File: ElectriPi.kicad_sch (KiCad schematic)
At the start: 56 parts, among them IC2 TPS51397ARJER, J1 2444, J2 JST XH 01x02, J3 JST XH 01x02, J6 Raspberry_Pi_2_3, J8 JST XH 01x02, Q1 SiA471DJ, Q2 SiA430DJT, U1 LM74700, U2 COOLING

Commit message: Add DigiKey PN's
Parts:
- C1, C11, C12, C2: DigiKey (none) -> 445-14428-2-ND
- C10, C13, C14, C15, C17, C6, C7, C8, C9: DigiKey (none) -> 490-GRM155R62A104KE14JTR-ND
- C18: DigiKey (none) -> 399-EEV107M050S9MAATR-ND
- C3: DigiKey (none) -> 1276-1860-2-ND
- C4, C5: DigiKey (none) -> 490-GRM31CR61A107MEA8KTR-ND
- D1: DigiKey (none) -> 112-XMC7K24CAHM3/ITR-ND
- D3, D5: DigiKey (none) -> 754-1124-2-ND
- D4: DigiKey (none) -> BZX84C13-FDITR-ND
- D6: DigiKey (none) -> 1727-2175-1-ND
- F1: DigiKey (none) -> F1889-ND
- IC2: DigiKey (none) -> 296-TPS51397ARJERTR-ND
- J2: DigiKey (none) -> 455-B2B-XH-A-ND
- L1: DigiKey (none) -> 541-1313-2-ND
- Q1: DigiKey (none) -> SIA471DJ-T1-GE3TR-ND
- Q2: DigiKey (none) -> 742-SIA430DJT-T1-GE3CT-ND
- R1, R11, R5: DigiKey (none) -> CR0402-FX-3302GLFTR-ND
- R12, R13, R7: DigiKey (none) -> CR0402-FX-1103GLFTR-ND
- R14: DigiKey (none) -> CR0402-FX-1502GLFTR-ND
- R3: DigiKey (none) -> CR0402-FX-1103GLFTR-ND; abv.Footprint 0402 -> (none)
- R4: DigiKey (none) -> CR0402-FX-1803GLFTR-ND
- R6: DigiKey (none) -> 311-1.00KLRTR-ND
- R8: DigiKey (none) -> CR0402-FX-1002GLFTR-ND
- U1: DigiKey (none) -> 296-LM74700QDBVRQ1CT-ND
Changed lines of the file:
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@@
+      (effects (font (size 1.27 1.27)) hide)
+    )
+    (property "DigiKey" "490-GRM155R62A104KE14JTR-ND" (at 102.235 43.18 0)
       (effects (font (size 1.27 1.27)) hide)
     )
@@
       (effects (font (size 1.27 1.27)) hide)
     )
+    (property "DigiKey" "754-1124-2-ND" (at 33.02 177.8 0)
+      (effects (font (size 1.27 1.27)) hide)
+    )
     (pin "1")
     (pin "2")
@@
     )
     (property "LCSC" "C1518754" (at 110.49 59.69 0)
+      (effects (font (size 1.27 1.27)) hide)
+    )
+    (property "DigiKey" "296-TPS51397ARJERTR-ND" (at 110.49 59.69 0)
       (effects (font (size 1.27 1.27)) hide)
     )
@@
       (effects (font (size 1.27 1.27)) hide)
     )
+    (property "DigiKey" "BZX84C13-FDITR-ND" (at 67.31 54.61 90)
+      (effects (font (size 1.27 1.27)) hide)
+    )
     (pin "1")
     (pin "2")
@@
     )
     (property "LCSC" "C2193622" (at 22.86 62.23 0)
+      (effects (font (size 1.27 1.27)) hide)
+    )
+    (property "DigiKey" "490-GRM155R62A104KE14JTR-ND" (at 22.86 62.23 0)
       (effects (font (size 1.27 1.27)) hide)
     )
@@
       (effects (font (size 1.27 1.27)) hide)
     )
+    (property "DigiKey" "490-GRM155R62A104KE14JTR-ND" (at 153.67 127 0)
+      (effects (font (size 1.27 1.27)) hide)
+    )
     (pin "1")
     (pin "2")
@@
       (effects (font (size 1.27 1.27)) hide)
     )
+    (property "DigiKey" "490-GRM155R62A104KE14JTR-ND" (at 186.69 55.88 0)
+      (effects (font (size 1.27 1.27)) hide)
+    )
     (pin "1")
     (pin "2")
@@
     )
     (property "LCSC" "C312983" (at 196.85 55.88 0)
+      (effects (font (size 1.27 1.27)) hide)
+    )
+    (property "DigiKey" "490-GRM31CR61A107MEA8KTR-ND" (at 196.85 55.88 0)
       (effects (font (size 1.27 1.27)) hide)
     )
@@
       (effects (font (size 1.27 1.27)) hide)
     )
+    (property "DigiKey" "CR0402-FX-3302GLFTR-ND" (at 156.21 74.93 0)
+      (effects (font (size 1.27 1.27)) hide)
+    )
     (pin "1")
     (pin "2")
@@
       (effects (font (size 1.27 1.27)) hide)
     )
+    (property "DigiKey" "445-14428-2-ND" (at 92.075 43.18 0)
+      (effects (font (size 1.27 1.27)) hide)
+    )
     (pin "1")
     (pin "2")
@@
     )
     (property "ManfNum" "CL10A105KB8NNNC" (at 139.7 35.56 0)
+      (effects (font (size 1.27 1.27)) hide)
+    )
+    (property "DigiKey" "1276-1860-2-ND" (at 139.7 35.56 0)
       (effects (font (size 1.27 1.27)) hide)
     )
@@
       (effects (font (size 1.27 1.27)) hide)
     )
+    (property "DigiKey" "399-EEV107M050S9MAATR-ND" (at 70.485 43.18 0)
+      (effects (font (size 1.27 1.27)) hide)
+    )
     (pin "1")
     (pin "2")
@@
     )
     (property "LCSC" "C2193622" (at 49.53 119.38 0)
+      (effects (font (size 1.27 1.27)) hide)
+    )
+    (property "DigiKey" "490-GRM155R62A104KE14JTR-ND" (at 49.53 119.38 0)
       (effects (font (size 1.27 1.27)) hide)
     )
@@
       (effects (font (size 1.27 1.27)) hide)
     )
+    (property "DigiKey" "490-GRM155R62A104KE14JTR-ND" (at 67.31 63.5 0)
+      (effects (font (size 1.27 1.27)) hide)
+    )
     (pin "1")
     (pin "2")
@@
       (effects (font (size 1.27 1.27)) hide)
     )
+    (property "DigiKey" "CR0402-FX-1002GLFTR-ND" (at 40.64 187.96 90)
+      (effects (font (size 1.27 1.27)) hide)
+    )
     (pin "1")
     (pin "2")
@@
       (effects (font (size 1.27 1.27)) hide)
     )
-    (property "abv.Footprint" "0402" (at 57.15 63.5 0)
-      (effects (font (size 1.27 1.27)) hide)
-    )
     (property "ManfNum" "" (at 57.15 63.5 0)
+      (effects (font (size 1.27 1.27)) hide)
+    )
+    (property "DigiKey" "CR0402-FX-1103GLFTR-ND" (at 57.15 63.5 0)
       (effects (font (size 1.27 1.27)) hide)
     )
@@
     )
     (property "LCSC" "C323721" (at 156.21 64.77 0)
+      (effects (font (size 1.27 1.27)) hide)
+    )
+    (property "DigiKey" "CR0402-FX-3302GLFTR-ND" (at 156.21 64.77 0)
       (effects (font (size 1.27 1.27)) hide)
     )
@@
       (effects (font (size 1.27 1.27)) hide)
     )
+    (property "DigiKey" "CR0402-FX-1803GLFTR-ND" (at 156.21 55.88 0)
+      (effects (font (size 1.27 1.27)) hide)
+    )
     (pin "1")
     (pin "2")
@@
     )
     (property "LCSC" "C319837" (at 217.17 63.5 0)
+      (effects (font (size 1.27 1.27)) hide)
+    )
+    (property "DigiKey" "CR0402-FX-1502GLFTR-ND" (at 217.17 63.5 0)
       (effects (font (size 1.27 1.27)) hide)
     )
@@
       (effects (font (size 1.27 1.27)) hide)
     )
+    (property "DigiKey" "CR0402-FX-1103GLFTR-ND" (at 156.21 69.85 0)
+      (effects (font (size 1.27 1.27)) hide)
+    )
     (pin "1")
     (pin "2")
@@
       (effects (font (size 1.27 1.27)) hide)
     )
+    (property "DigiKey" "SIA471DJ-T1-GE3TR-ND" (at 57.15 43.18 90)
+      (effects (font (size 1.27 1.27)) hide)
+    )
     (pin "1")
     (pin "3")
@@
       (effects (font (size 1.27 1.27)) hide)
     )
+    (property "DigiKey" "311-1.00KLRTR-ND" (at 40.64 177.8 90)
+      (effects (font (size 1.27 1.27)) hide)
+    )
     (pin "1")
     (pin "2")
@@
       (effects (font (size 1.27 1.27)) hide)
     )
+    (property "DigiKey" "CR0402-FX-3302GLFTR-ND" (at 166.37 59.69 90)
+      (effects (font (size 1.27 1.27)) hide)
+    )
     (pin "1")
     (pin "2")
@@
       (effects (font (size 1.27 1.27)) hide)
     )
+    (property "DigiKey" "445-14428-2-ND" (at 80.01 121.92 0)
+      (effects (font (size 1.27 1.27)) hide)
+    )
     (pin "1")
     (pin "2")
@@
     )
     (property "LCSC" "C2193622" (at 139.7 177.8 0)
+      (effects (font (size 1.27 1.27)) hide)
+    )
+    (property "DigiKey" "490-GRM155R62A104KE14JTR-ND" (at 139.7 177.8 0)
       (effects (font (size 1.27 1.27)) hide)
     )
@@
       (effects (font (size 1.27 1.27)) hide)
     )
+    (property "DigiKey" "455-B2B-XH-A-ND" (at 31.75 78.74 90)
+      (effects (font (size 1.27 1.27)) hide)
+    )
     (pin "1")
     (pin "2")
@@
       (effects (font (size 1.27 1.27)) hide)
     )
+    (property "DigiKey" "CR0402-FX-1103GLFTR-ND" (at 217.17 55.88 0)
+      (effects (font (size 1.27 1.27)) hide)
+    )
     (pin "1")
     (pin "2")
@@
     )
     (property "ManfNum" "" (at 36.83 40.64 0)
+      (effects (font (size 1.27 1.27)) hide)
+    )
+    (property "DigiKey" "F1889-ND" (at 36.83 40.64 90)
       (effects (font (size 1.27 1.27)) hide)
     )
@@
       (effects (font (size 1.27 1.27)) hide)
     )
+    (property "DigiKey" "754-1124-2-ND" (at 33.02 187.96 0)
+      (effects (font (size 1.27 1.27)) hide)
+    )
     (pin "1")
     (pin "2")
@@
       (effects (font (size 1.27 1.27)) hide)
     )
+    (property "DigiKey" "445-14428-2-ND" (at 90.805 121.92 0)
+      (effects (font (size 1.27 1.27)) hide)
+    )
     (pin "1")
     (pin "2")
@@
     )
     (property "LCSC" "C477955" (at 22.86 127 0)
+      (effects (font (size 1.27 1.27)) hide)
+    )
+    (property "DigiKey" "1727-2175-1-ND" (at 22.86 127 90)
       (effects (font (size 1.27 1.27)) hide)
     )
@@
       (effects (font (size 1.27 1.27)) hide)
     )
+    (property "DigiKey" "490-GRM155R62A104KE14JTR-ND" (at 177.8 40.64 0)
+      (effects (font (size 1.27 1.27)) hide)
+    )
     (pin "1")
     (pin "2")
@@
     )
     (property "LCSC" "C312983" (at 207.01 55.88 0)
+      (effects (font (size 1.27 1.27)) hide)
+    )
+    (property "DigiKey" "490-GRM31CR61A107MEA8KTR-ND" (at 207.01 55.88 0)
       (effects (font (size 1.27 1.27)) hide)
     )
@@
     )
     (property "LCSC" "C413107" (at 128.27 95.25 0)
+      (effects (font (size 1.27 1.27)) hide)
+    )
+    (property "DigiKey" "CR0402-FX-1103GLFTR-ND" (at 128.27 95.25 0)
       (effects (font (size 1.27 1.27)) hide)
     )
@@
     )
     (property "Mouser" "70-IHLP4040DZER1R8M1" (at 182.88 50.8 90)
+      (effects (font (size 1.27 1.27)) hide)
+    )
+    (property "DigiKey" "541-1313-2-ND" (at 182.88 50.8 90)
       (effects (font (size 1.27 1.27)) hide)
     )
@@
       (effects (font (size 1.27 1.27)) hide)
     )
+    (property "DigiKey" "490-GRM155R62A104KE14JTR-ND" (at 46.99 130.81 0)
+      (effects (font (size 1.27 1.27)) hide)
+    )
     (pin "1")
     (pin "2")
@@
     )
     (property "LCSC" "C2179409" (at 81.915 43.18 0)
+      (effects (font (size 1.27 1.27)) hide)
+    )
+    (property "DigiKey" "445-14428-2-ND" (at 81.915 43.18 0)
       (effects (font (size 1.27 1.27)) hide)
     )
@@
       (effects (font (size 1.27 1.27)) hide)
     )
+    (property "DigiKey" "112-XMC7K24CAHM3/ITR-ND" (at 41.91 48.26 90)
+      (effects (font (size 1.27 1.27)) hide)
+    )
     (pin "1")
     (pin "2")
@@
       (effects (font (size 1.27 1.27)) hide)
     )
+    (property "DigiKey" "742-SIA430DJT-T1-GE3CT-ND" (at 66.04 119.38 90)
+      (effects (font (size 1.27 1.27)) hide)
+    )
     (pin "1")
     (pin "3")
@@
       (effects (font (size 1.27 1.27)) hide)
     )
+    (property "DigiKey" "296-LM74700QDBVRQ1CT-ND" (at 66.04 134.62 0)
+      (effects (font (size 1.27 1.27)) hide)
+    )

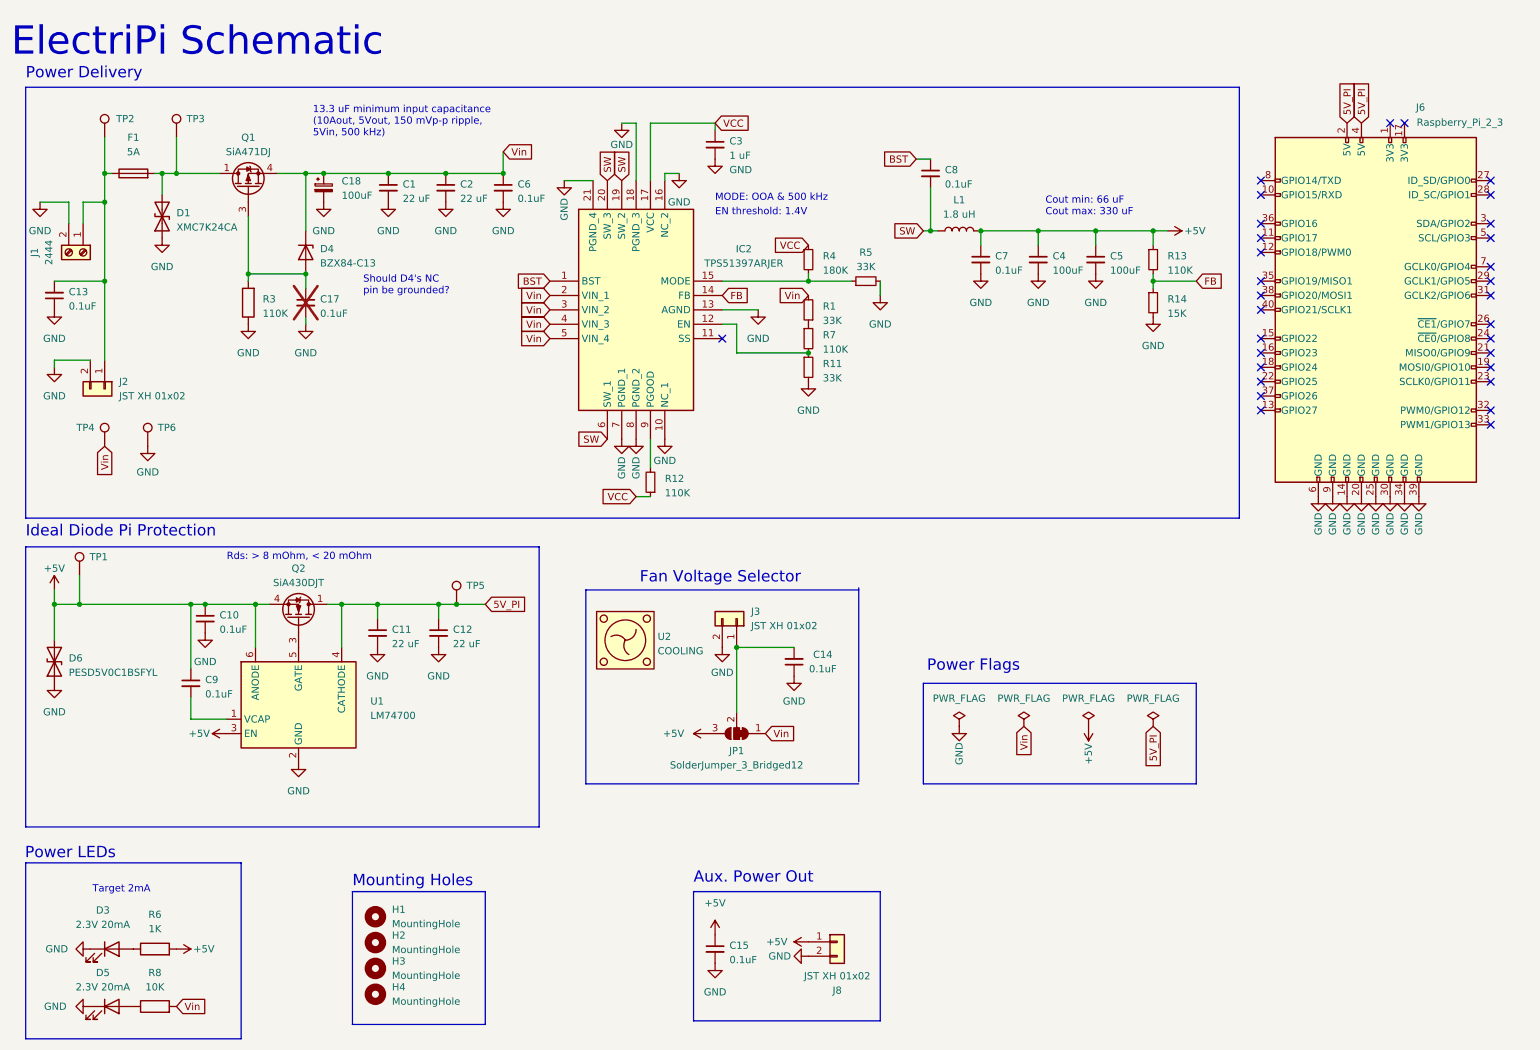
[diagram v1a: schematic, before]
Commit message: Change input connector to 5.08mm pitch. DNP caps on connectors. Remove JLC silk
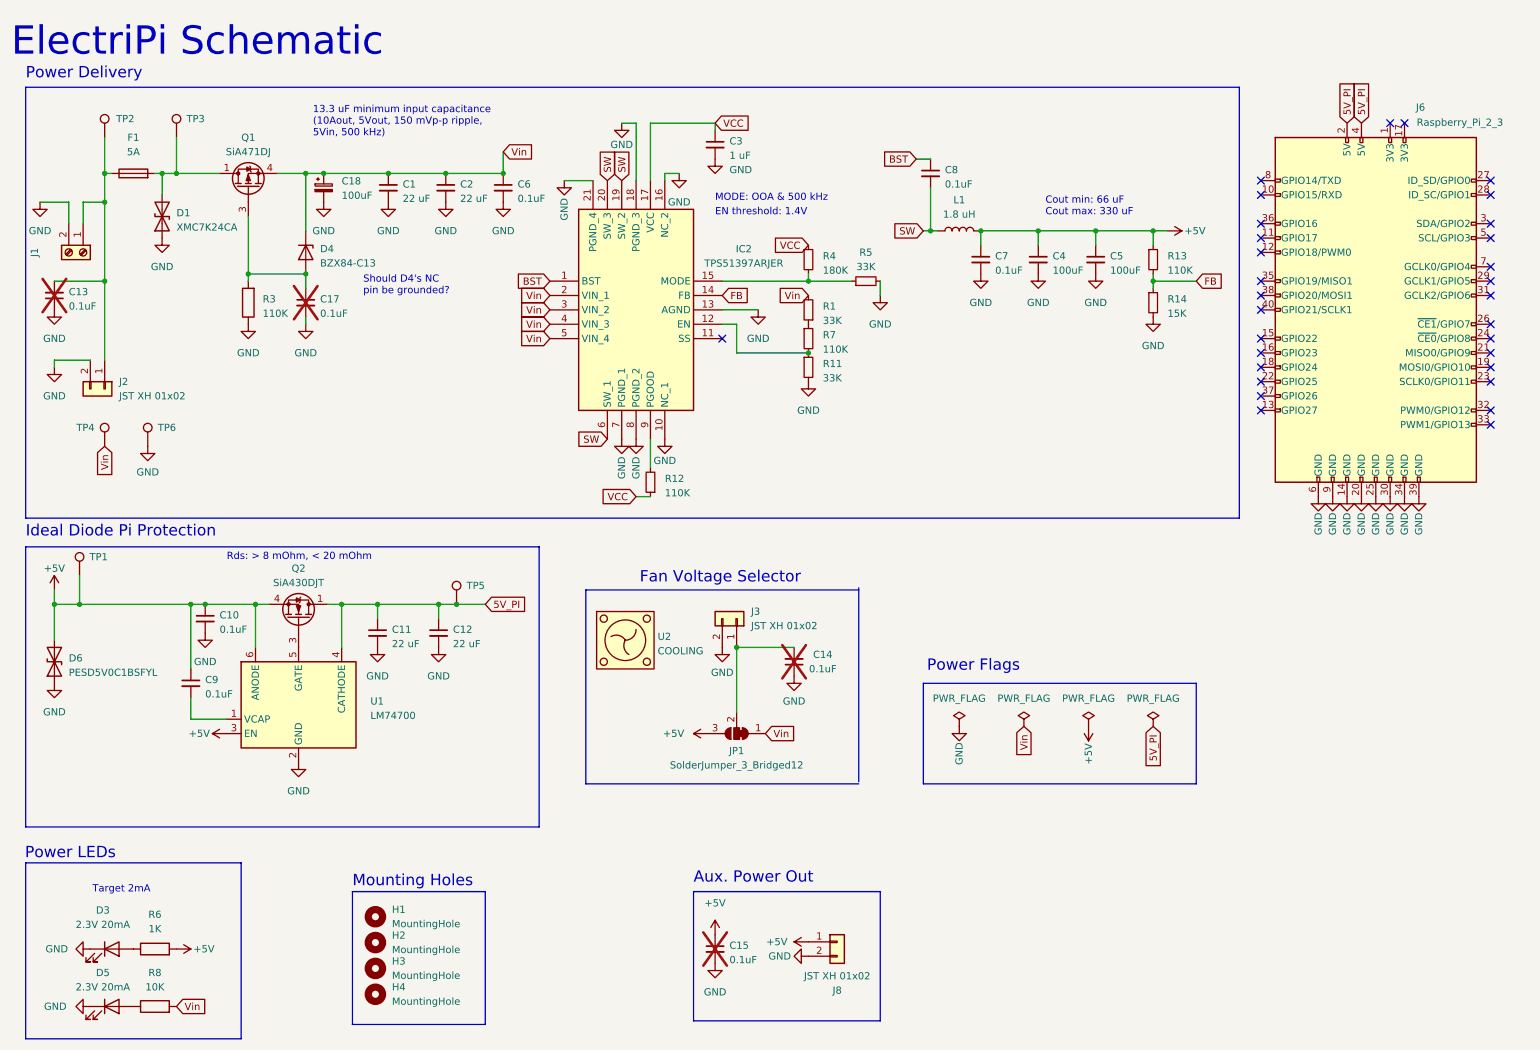
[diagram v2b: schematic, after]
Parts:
- C13, C14, C15: now not fitted
- J1: value 2444 -> 282837-2; footprint TerminalBlock_4Ucon:TerminalBlock_4Ucon_1x02_P3.50mm_Horizontal -> TerminalBlock:TerminalBlock_bornier-2_P5.08mm; DigiKey (none) -> A113320-ND; LCSC C123214 -> (none)
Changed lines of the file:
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@@
   )
   (symbol (lib_id "Device:C_Small") (at 22.86 62.23 180) (unit 1)
-    (in_bom yes) (on_board yes) (dnp no) (fields_autoplaced)
+    (in_bom yes) (on_board yes) (dnp yes) (fields_autoplaced)
     (property "Reference" "C13" (at 25.4 61.5886 0)
       (effects (font (size 1.27 1.27)) (justify right))
@@
   )
   (symbol (lib_id "Device:C_Small") (at 153.67 127 180) (unit 1)
-    (in_bom yes) (on_board yes) (dnp no)
+    (in_bom yes) (on_board yes) (dnp yes)
     (property "Reference" "C14" (at 158.75 125.73 0)
       (effects (font (size 1.27 1.27)))
@@
       (effects (font (size 1.27 1.27)))
     )
-    (property "Value" "2444" (at 21.8948 54.61 0)
-      (effects (font (size 1.27 1.27)))
-    )
-    (property "Footprint" "TerminalBlock_4Ucon:TerminalBlock_4Ucon_1x02_P3.50mm_Horizontal" (at 27.94 54.61 0)
+    (property "Value" "282837-2" (at 21.8948 54.61 0)
+      (effects (font (size 1.27 1.27)) hide)
+    )
+    (property "Footprint" "TerminalBlock:TerminalBlock_bornier-2_P5.08mm" (at 27.94 54.61 0)
       (effects (font (size 1.27 1.27)) hide)
     )
@@
       (effects (font (size 1.27 1.27)) hide)
     )
-    (property "LCSC" "C123214" (at 27.94 54.61 0)
+    (property "LCSC" "" (at 27.94 54.61 0)
       (effects (font (size 1.27 1.27)) hide)
     )
     (property "PCBway" "" (at 27.94 54.61 0)
+      (effects (font (size 1.27 1.27)) hide)
+    )
+    (property "DigiKey" "A113320-ND" (at 27.94 54.61 0)
       (effects (font (size 1.27 1.27)) hide)
     )
@@
   )
   (symbol (lib_id "Device:C_Small") (at 139.7 177.8 0) (unit 1)
-    (in_bom yes) (on_board yes) (dnp no) (fields_autoplaced)
+    (in_bom yes) (on_board yes) (dnp yes) (fields_autoplaced)
     (property "Reference" "C15" (at 142.24 177.1713 0)
       (effects (font (size 1.27 1.27)) (justify left))
